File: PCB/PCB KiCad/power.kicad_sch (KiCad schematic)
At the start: 0 parts

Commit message: draw schematic for 60%
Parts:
- added C? (x6): C, Capacitor_SMD:C_0805_2012Metric_Pad1.18x1.45mm_HandSolder, symbol Device:C
- added FB?: FerriteBead, symbol Device:FerriteBead
- added R?: R, Resistor_SMD:R_0805_2012Metric_Pad1.20x1.40mm_HandSolder, symbol Device:R
- added U?: LM285D-2.5, Package_SO:SOIC-8_3.9x4.9mm_P1.27mm, symbol Reference_Voltage:LM285D-2.5
- added U?: AMS1117-3.3, Package_TO_SOT_SMD:SOT-223-3_TabPin2, symbol Regulator_Linear:AMS1117-3.3
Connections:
- new net: C?.1, C?.1, U?.2 (VO)
- new net: C?.1, R?.2, U?.8 (K)
- new net: C?.1, FB?.2
- new net +5V: C?.1, C?.1, FB?.1, U?.3 (VI)
- new net GND: C?.2, C?.2, C?.2, C?.2, C?.2, C?.2, U?.1 (GND), U?.4 (A)
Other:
- note added: "+3.3v"
- note added: "2.5v reference"
- note added: "Main Power Supply +5V"
- note added: "TO DO: Nets 5v prefilter?"

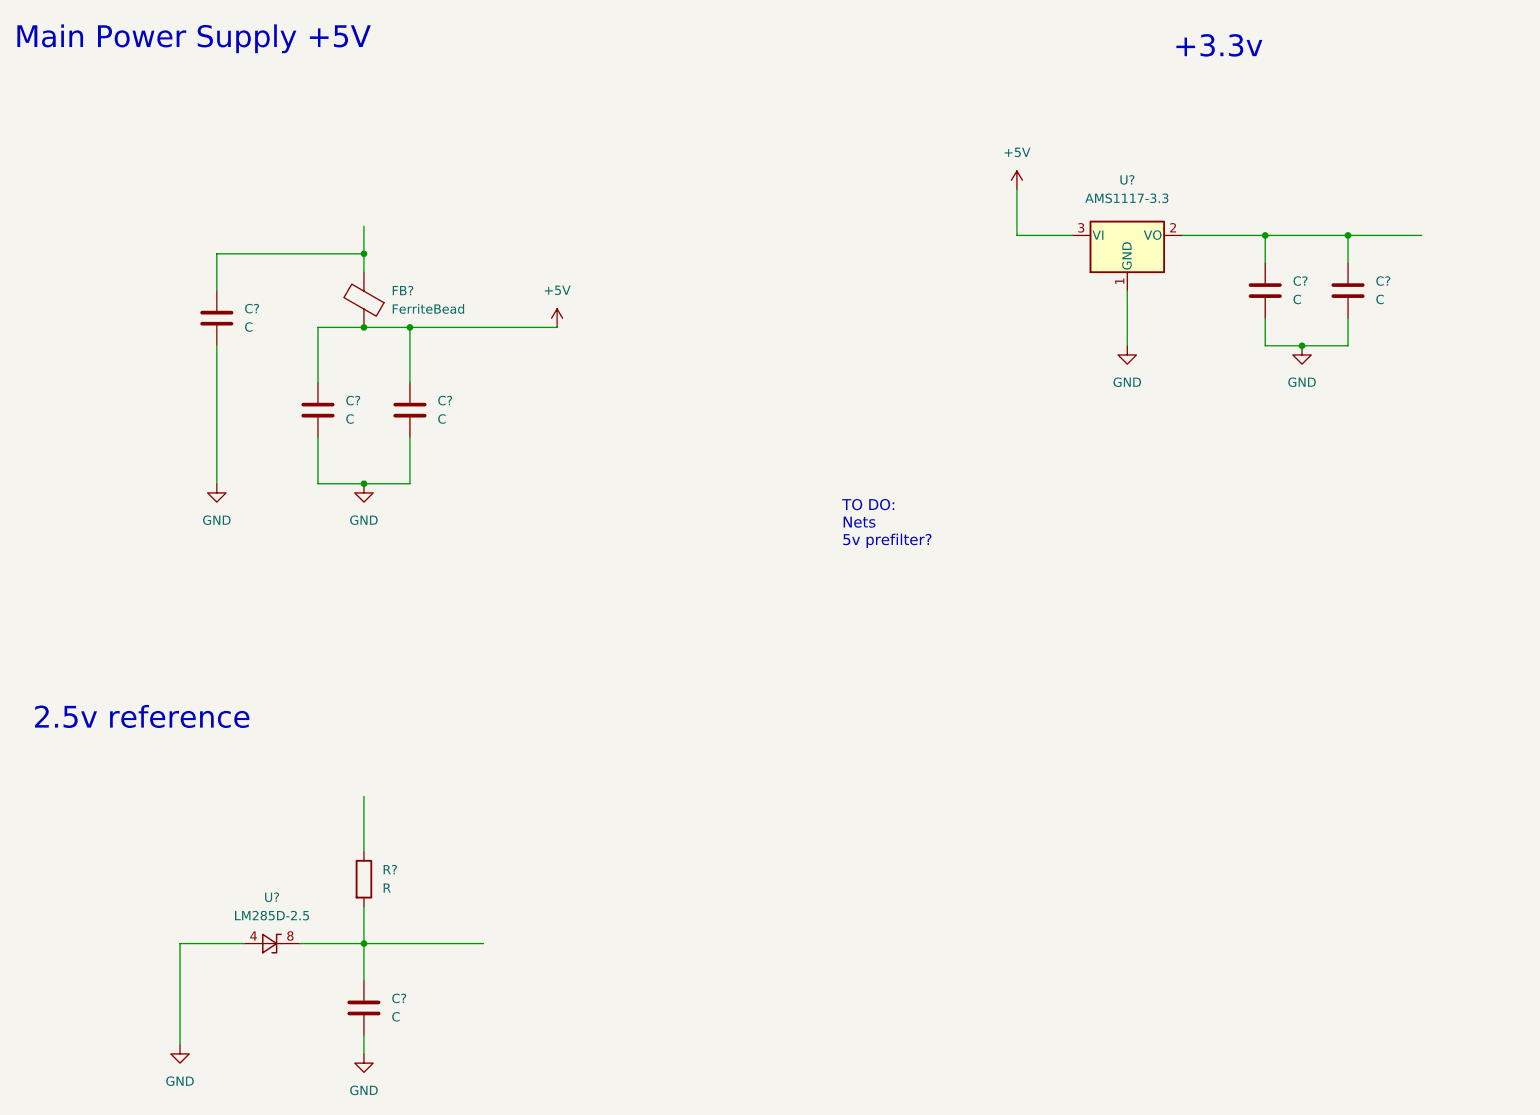
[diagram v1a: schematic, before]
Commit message: Add buttons: MCU RESET, TRIGGER
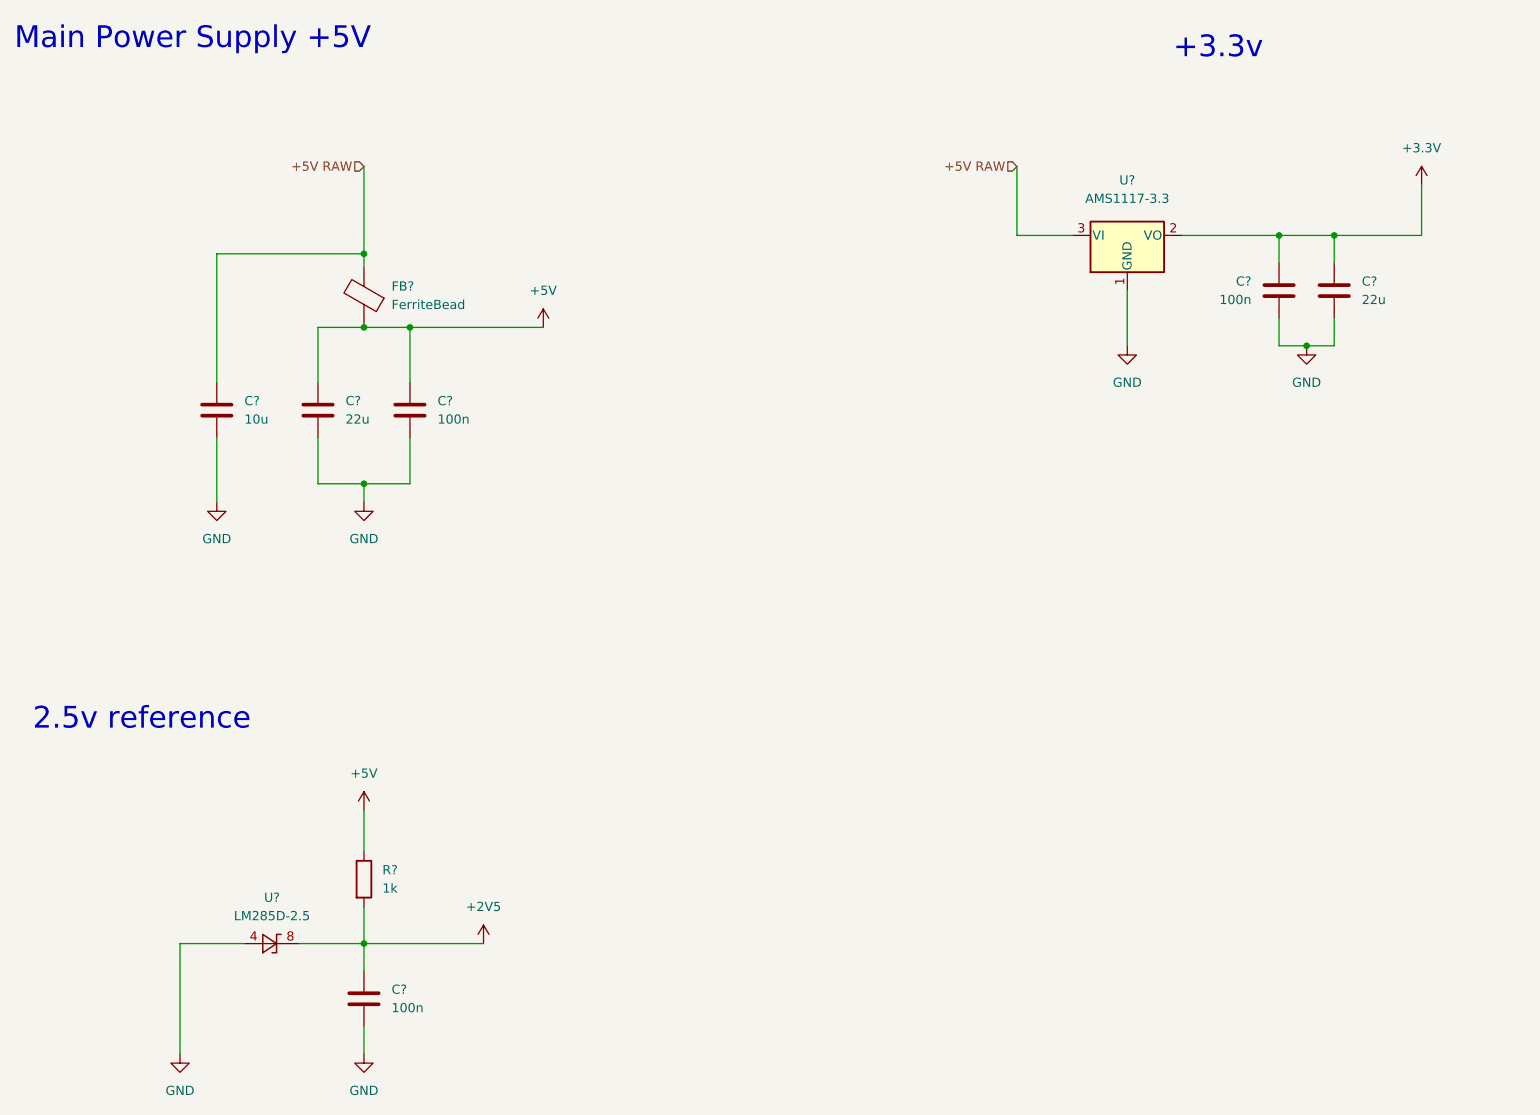
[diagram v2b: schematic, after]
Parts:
- C? (x2): value C -> 22u
- C? (x3): value C -> 100n
- C?: value C -> 10u
- R?: value R -> 1k
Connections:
- net +5V: now also R?.1; no longer U?.3 (VI)
- net GND: now also C?.1; no longer C?.2
- net +3V3: now reaches C?.1, U?.2 (VO)
- net +3V3: now also C?.2; no longer C?.1
- net +2V5: now reaches C?.1, R?.2, U?.8 (K)
- net +5V RAW: now reaches C?.1, FB?.2
- net +5V RAW: now also U?.3 (VI)
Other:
- note removed: "TO DO: Nets 5v prefilter?"
- moved on the sheet: C?, FB?

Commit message: ERC: add power flags to satisfy the ERC crap
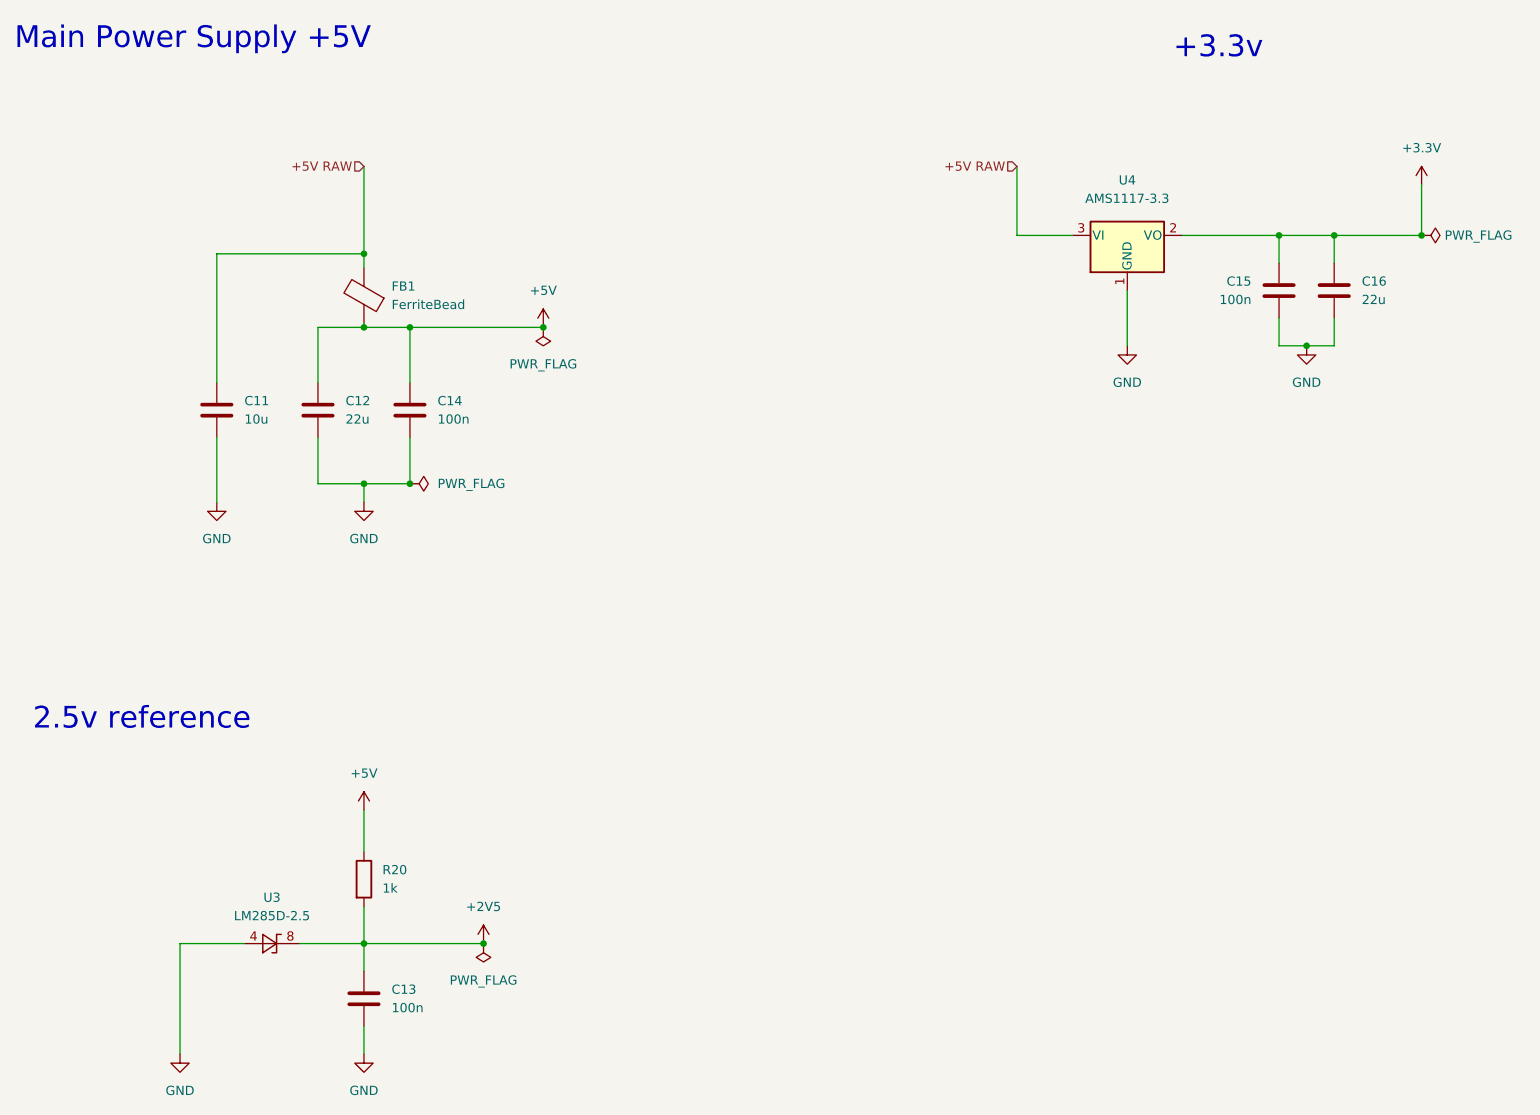
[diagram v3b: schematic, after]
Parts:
- gave numbers to parts that had none: 10
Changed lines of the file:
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@@
   (junction (at 83.82 66.04) (diameter 0) (color 0 0 0 0)
   )
+  (junction (at 229.87 63.5) (diameter 0) (color 0 0 0 0)
+  )
   (junction (at 83.82 76.2) (diameter 0) (color 0 0 0 0)
   )
@@
   )
   (junction (at 217.805 63.5) (diameter 0) (color 0 0 0 0)
+  )
+  (junction (at 100.33 161.29) (diameter 0) (color 0 0 0 0)
+  )
+  (junction (at 108.585 76.2) (diameter 0) (color 0 0 0 0)
+  )
+  (junction (at 90.17 97.79) (diameter 0) (color 0 0 0 0)
   )
   (junction (at 213.995 78.74) (diameter 0) (color 0 0 0 0)
@@
   (symbol (lib_id "Device:C") (at 217.805 71.12 0) (unit 1)
     (in_bom yes) (on_board yes) (fields_autoplaced)
-    (property "Reference" "C?" (id 0) (at 221.615 69.8499 0)
+    (property "Reference" "C16" (id 0) (at 221.615 69.8499 0)
       (effects (font (size 1.27 1.27)) (justify left))
     )
@@
     (pin "2")
   )
+  (symbol (lib_id "power:PWR_FLAG") (at 108.585 76.2 0) (mirror x) (unit 1)
+    (in_bom yes) (on_board yes) (fields_autoplaced)
+    (property "Reference" "#FLG0101" (id 0) (at 108.585 78.105 0)
+      (effects (font (size 1.27 1.27)) hide)
+    )
+    (property "Value" "PWR_FLAG" (id 1) (at 108.585 81.28 0))
+    (property "Footprint" "" (id 2) (at 108.585 76.2 0)
+      (effects (font (size 1.27 1.27)) hide)
+    )
+    (property "Datasheet" "~" (id 3) (at 108.585 76.2 0)
+      (effects (font (size 1.27 1.27)) hide)
+    )
+    (pin "1")
+  )
   (symbol (lib_id "Device:C") (at 90.17 87.63 0) (unit 1)
     (in_bom yes) (on_board yes) (fields_autoplaced)
-    (property "Reference" "C?" (id 0) (at 93.98 86.3599 0)
+    (property "Reference" "C14" (id 0) (at 93.98 86.3599 0)
       (effects (font (size 1.27 1.27)) (justify left))
     )
@@
   (symbol (lib_id "power:GND") (at 58.42 176.53 0) (unit 1)
     (in_bom yes) (on_board yes) (fields_autoplaced)
-    (property "Reference" "#PWR?" (id 0) (at 58.42 182.88 0)
+    (property "Reference" "#PWR024" (id 0) (at 58.42 182.88 0)
       (effects (font (size 1.27 1.27)) hide)
     )
@@
   (symbol (lib_id "Reference_Voltage:LM285D-2.5") (at 71.12 161.29 0) (unit 1)
     (in_bom yes) (on_board yes) (fields_autoplaced)
-    (property "Reference" "U?" (id 0) (at 71.12 154.94 0))
+    (property "Reference" "U3" (id 0) (at 71.12 154.94 0))
     (property "Value" "LM285D-2.5" (id 1) (at 71.12 157.48 0))
     (property "Footprint" "Package_SO:SOIC-8_3.9x4.9mm_P1.27mm" (id 2) (at 71.12 166.37 0)
@@
   (symbol (lib_id "power:GND") (at 213.995 78.74 0) (unit 1)
     (in_bom yes) (on_board yes) (fields_autoplaced)
-    (property "Reference" "#PWR?" (id 0) (at 213.995 85.09 0)
+    (property "Reference" "#PWR032" (id 0) (at 213.995 85.09 0)
       (effects (font (size 1.27 1.27)) hide)
     )
@@
   (symbol (lib_id "Device:C") (at 83.82 168.91 0) (unit 1)
     (in_bom yes) (on_board yes) (fields_autoplaced)
-    (property "Reference" "C?" (id 0) (at 87.63 167.6399 0)
+    (property "Reference" "C13" (id 0) (at 87.63 167.6399 0)
       (effects (font (size 1.27 1.27)) (justify left))
     )
@@
   (symbol (lib_id "Device:C") (at 210.185 71.12 0) (mirror x) (unit 1)
     (in_bom yes) (on_board yes) (fields_autoplaced)
-    (property "Reference" "C?" (id 0) (at 206.375 69.8499 0)
+    (property "Reference" "C15" (id 0) (at 206.375 69.8499 0)
       (effects (font (size 1.27 1.27)) (justify right))
     )
@@
     (pin "2")
   )
+  (symbol (lib_id "power:PWR_FLAG") (at 100.33 161.29 0) (mirror x) (unit 1)
+    (in_bom yes) (on_board yes) (fields_autoplaced)
+    (property "Reference" "#FLG?" (id 0) (at 100.33 163.195 0)
+      (effects (font (size 1.27 1.27)) hide)
+    )
+    (property "Value" "PWR_FLAG" (id 1) (at 100.33 166.37 0))
+    (property "Footprint" "" (id 2) (at 100.33 161.29 0)
+      (effects (font (size 1.27 1.27)) hide)
+    )
+    (property "Datasheet" "~" (id 3) (at 100.33 161.29 0)
+      (effects (font (size 1.27 1.27)) hide)
+    )
+    (pin "1")
+  )
   (symbol (lib_id "Device:R") (at 83.82 152.4 0) (unit 1)
     (in_bom yes) (on_board yes) (fields_autoplaced)
-    (property "Reference" "R?" (id 0) (at 86.36 151.1299 0)
+    (property "Reference" "R20" (id 0) (at 86.36 151.1299 0)
       (effects (font (size 1.27 1.27)) (justify left))
     )
@@
   (symbol (lib_id "power:+5V") (at 83.82 142.875 0) (unit 1)
     (in_bom yes) (on_board yes)
-    (property "Reference" "#PWR?" (id 0) (at 83.82 146.685 0)
+    (property "Reference" "#PWR027" (id 0) (at 83.82 146.685 0)
       (effects (font (size 1.27 1.27)) hide)
     )
@@
   (symbol (lib_id "Device:C") (at 77.47 87.63 0) (unit 1)
     (in_bom yes) (on_board yes) (fields_autoplaced)
-    (property "Reference" "C?" (id 0) (at 81.28 86.3599 0)
+    (property "Reference" "C12" (id 0) (at 81.28 86.3599 0)
       (effects (font (size 1.27 1.27)) (justify left))
     )
@@
   (symbol (lib_id "power:+2V5") (at 100.33 161.29 0) (unit 1)
     (in_bom yes) (on_board yes) (fields_autoplaced)
-    (property "Reference" "#PWR?" (id 0) (at 100.33 165.1 0)
+    (property "Reference" "#PWR029" (id 0) (at 100.33 165.1 0)
       (effects (font (size 1.27 1.27)) hide)
     )
@@
     (pin "1")
   )
+  (symbol (lib_id "power:PWR_FLAG") (at 229.87 63.5 270) (mirror x) (unit 1)
+    (in_bom yes) (on_board yes) (fields_autoplaced)
+    (property "Reference" "#FLG?" (id 0) (at 231.775 63.5 0)
+      (effects (font (size 1.27 1.27)) hide)
+    )
+    (property "Value" "PWR_FLAG" (id 1) (at 233.045 63.4999 90)
+      (effects (font (size 1.27 1.27)) (justify left))
+    )
+    (property "Footprint" "" (id 2) (at 229.87 63.5 0)
+      (effects (font (size 1.27 1.27)) hide)
+    )
+    (property "Datasheet" "~" (id 3) (at 229.87 63.5 0)
+      (effects (font (size 1.27 1.27)) hide)
+    )
+    (pin "1")
+  )
   (symbol (lib_id "power:+5V") (at 108.585 76.2 0) (unit 1)
     (in_bom yes) (on_board yes) (fields_autoplaced)
-    (property "Reference" "#PWR?" (id 0) (at 108.585 80.01 0)
+    (property "Reference" "#PWR030" (id 0) (at 108.585 80.01 0)
       (effects (font (size 1.27 1.27)) hide)
     )
@@
   (symbol (lib_id "power:+3.3V") (at 229.87 56.515 0) (unit 1)
     (in_bom yes) (on_board yes) (fields_autoplaced)
-    (property "Reference" "#PWR?" (id 0) (at 229.87 60.325 0)
+    (property "Reference" "#PWR033" (id 0) (at 229.87 60.325 0)
       (effects (font (size 1.27 1.27)) hide)
     )
@@
   (symbol (lib_id "power:GND") (at 63.5 100.33 0) (unit 1)
     (in_bom yes) (on_board yes) (fields_autoplaced)
-    (property "Reference" "#PWR?" (id 0) (at 63.5 106.68 0)
+    (property "Reference" "#PWR025" (id 0) (at 63.5 106.68 0)
       (effects (font (size 1.27 1.27)) hide)
     )
@@
   (symbol (lib_id "Regulator_Linear:AMS1117-3.3") (at 189.23 63.5 0) (unit 1)
     (in_bom yes) (on_board yes) (fields_autoplaced)
-    (property "Reference" "U?" (id 0) (at 189.23 55.88 0))
+    (property "Reference" "U4" (id 0) (at 189.23 55.88 0))
     (property "Value" "AMS1117-3.3" (id 1) (at 189.23 58.42 0))
     (property "Footprint" "Package_TO_SOT_SMD:SOT-223-3_TabPin2" (id 2) (at 189.23 58.42 0)
@@
   (symbol (lib_id "power:GND") (at 83.82 100.33 0) (unit 1)
     (in_bom yes) (on_board yes) (fields_autoplaced)
-    (property "Reference" "#PWR?" (id 0) (at 83.82 106.68 0)
+    (property "Reference" "#PWR026" (id 0) (at 83.82 106.68 0)
       (effects (font (size 1.27 1.27)) hide)
     )
@@
   (symbol (lib_id "Device:C") (at 63.5 87.63 0) (unit 1)
     (in_bom yes) (on_board yes) (fields_autoplaced)
-    (property "Reference" "C?" (id 0) (at 67.31 86.3599 0)
+    (property "Reference" "C11" (id 0) (at 67.31 86.3599 0)
       (effects (font (size 1.27 1.27)) (justify left))
     )
@@
   (symbol (lib_id "power:GND") (at 189.23 78.74 0) (unit 1)
     (in_bom yes) (on_board yes) (fields_autoplaced)
-    (property "Reference" "#PWR?" (id 0) (at 189.23 85.09 0)
+    (property "Reference" "#PWR031" (id 0) (at 189.23 85.09 0)
       (effects (font (size 1.27 1.27)) hide)
     )
@@
   (symbol (lib_id "Device:FerriteBead") (at 83.82 71.755 180) (unit 1)
     (in_bom yes) (on_board yes) (fields_autoplaced)
-    (property "Reference" "FB?" (id 0) (at 87.63 70.5357 0)
+    (property "Reference" "FB1" (id 0) (at 87.63 70.5357 0)
       (effects (font (size 1.27 1.27)) (justify right))
     )
@@
     (pin "2")
   )
+  (symbol (lib_id "power:PWR_FLAG") (at 90.17 97.79 270) (mirror x) (unit 1)
+    (in_bom yes) (on_board yes) (fields_autoplaced)
+    (property "Reference" "#FLG0102" (id 0) (at 92.075 97.79 0)
+      (effects (font (size 1.27 1.27)) hide)
+    )
+    (property "Value" "PWR_FLAG" (id 1) (at 93.98 97.7899 90)
+      (effects (font (size 1.27 1.27)) (justify left))
+    )
+    (property "Footprint" "" (id 2) (at 90.17 97.79 0)
+      (effects (font (size 1.27 1.27)) hide)
+    )
+    (property "Datasheet" "~" (id 3) (at 90.17 97.79 0)
+      (effects (font (size 1.27 1.27)) hide)
+    )
+    (pin "1")
+  )
   (symbol (lib_id "power:GND") (at 83.82 176.53 0) (unit 1)
     (in_bom yes) (on_board yes) (fields_autoplaced)
-    (property "Reference" "#PWR?" (id 0) (at 83.82 182.88 0)
-      (effects (font (size 1.27 1.27)) hide)
-    )
+    (property "Reference" "#PWR028" (id 0) (at 83.82 182.88 0)
+      (effects (font (size 1.27 1.27)) hide)
+    )
